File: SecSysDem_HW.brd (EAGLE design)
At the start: 99 x 80 mm, 49 parts, among them IC1 L7805 5V, Q1 2N3904, T1 MOSFET_NCHANNEL_ENHANCEMENT2N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, T2 MOSFET_NCHANNEL_ENHANCEMENT2N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, T3 MOSFET_NCHANNEL_ENHANCEMENT2N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, U1 XPLAINED_MINI_PINOUT, U2 PCF8574_IO_EXPANDER, U4 FT24C512A, U5 MCP4901-E/SN, X1 C-GRID-06-70553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

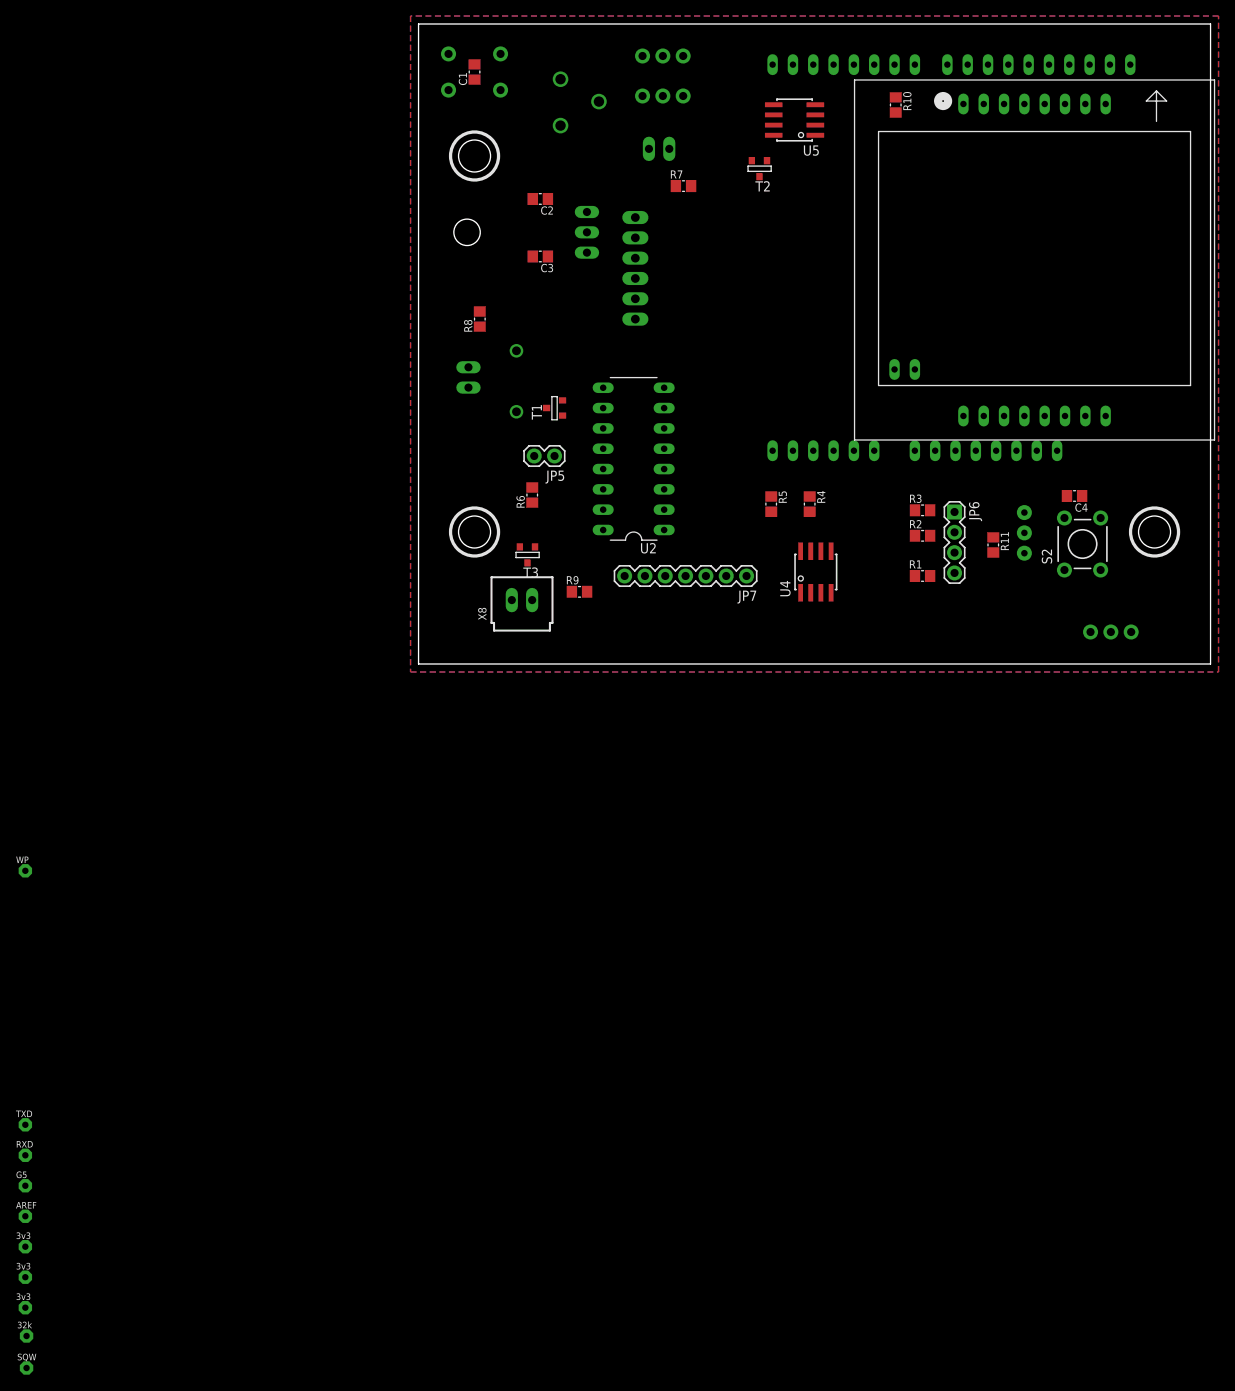
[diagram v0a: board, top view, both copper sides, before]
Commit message: Continued PCB layout. Moved some pin options.
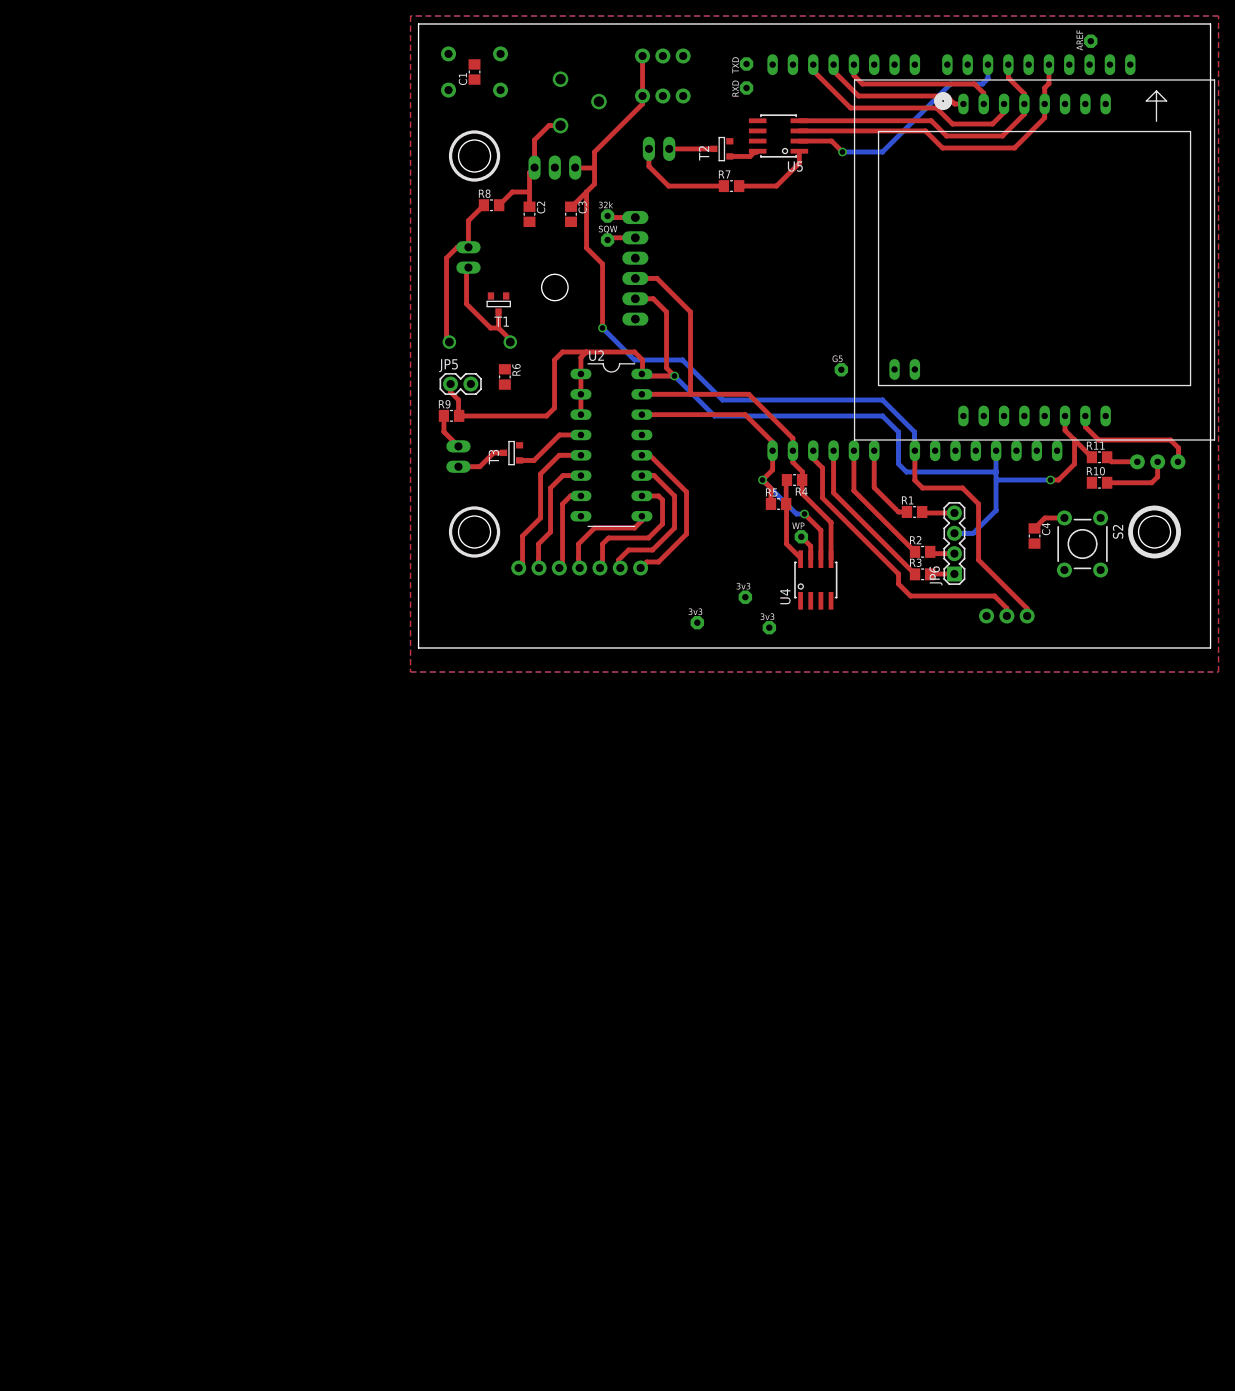
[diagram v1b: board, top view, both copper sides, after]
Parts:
- moved V6 198.3 mm to (84.0, 66.8), turned to 90 degrees
- moved V4 161.0 mm to (41.0, 61.0), turned to 90 degrees
- moved V3 160.3 mm to (41.0, 64.0), turned to 90 degrees
- moved V10 158.6 mm to (23.6, 42.0)
- moved V2 157.7 mm to (23.6, 45.0)
- moved V5 144.2 mm to (52.9, 25.8)
- moved V9 126.0 mm to (43.9, -6.46)
- moved V8 123.8 mm to (40.9, -2.65)
- moved V7 114.6 mm to (34.9, -5.84)
- moved V1 105.6 mm to (47.9, 4.90)
- moved R10 53.7 mm to (85.1, 11.7), turned to 0 degrees
- moved JP7 28.5 mm to (12.5, 1.00), flipped to the bottom
- moved R9 27.2 mm to (4.12, 20.0)
- moved X8 19.6 mm to (4.99, 14.9), flipped to the bottom, turned to 90 degrees
- moved Q1 18.9 mm to (92.4, 14.3), turned to 180 degrees
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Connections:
- net BELL_RINGER: now also U2.4; no longer U1.P$21
- net PUSH_BUTTON: now also U1.P$21; no longer U2.4
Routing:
- net +3V3: track 0.00 -> 168.1 mm, vias 0 -> 2
- net +5V: track 0.00 -> 119.0 mm, vias 0 -> 1
- net I2C_SDA: track 0.00 -> 57.2 mm
- net SPI_SCK: track 0.00 -> 40.0 mm
- net I2C_SCL: track 0.00 -> 40.0 mm, vias 0 -> 2
- net SPI_MOSI: track 0.00 -> 37.1 mm
- net PIR_SENSOR: track 0.00 -> 36.8 mm
- net !DAC_CS: track 0.00 -> 29.7 mm, vias 0 -> 1
- net LCD_DC: track 0.00 -> 29.0 mm
- net KEYPAD_7: track 0.00 -> 20.2 mm
- net N$17: track 0.00 -> 20.0 mm
- net LCD_SS: track 0.00 -> 19.8 mm
- net RGB_BLU: track 0.00 -> 19.7 mm
- net KEYPAD_1: track 0.00 -> 18.9 mm
- net KEYPAD_6: track 0.00 -> 18.9 mm
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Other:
- board size 99 x 80 mm -> 99 x 78 mm

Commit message: Finished PCB layout.
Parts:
- added R12, R13, R14, R15, R16, R17, R18: 10k, Luke:C0805
- moved V7 41.1 mm to (73.8, 7.16)
- moved V9 41.0 mm to (14.8, 22.5)
- moved R10 5.00 mm to (90.1, 11.7)
- moved V8 3.16 mm to (37.9, -1.65)
- moved JP7 2.00 mm to (12.5, -1.00)
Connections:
- net +3V3: now also R12.2, R13.2, R14.2, R15.2, R16.2, R17.2, R18.2
- net KEYPAD_1: now also R12.1
- net KEYPAD_2: now also R13.1
- net KEYPAD_3: now also R14.1
- net KEYPAD_4: now also R15.1
- net KEYPAD_5: now also R16.1
- net KEYPAD_6: now also R17.1
- net KEYPAD_7: now also R18.1
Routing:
- net !RESET_BTN: track 0.00 -> 129.4 mm, vias 0 -> 3
- net DOORLOCK_SOLENOID: track 0.00 -> 90.6 mm, vias 0 -> 1
- net +3V3: track 168.1 -> 254.7 mm, vias 2 -> 5
- net PUSH_BUTTON: track 4.28 -> 82.0 mm
- net LCD_BACKLIGHT: track 0.00 -> 74.5 mm, vias 0 -> 1
- net PHOTORESISTOR: track 0.00 -> 62.3 mm, vias 0 -> 1
- net DOOR_HALL_EFFECT: track 0.00 -> 39.7 mm
- net WINDOW_HALL_EFFECT: track 0.00 -> 37.4 mm
- net I2C_SCL: track 40.0 -> 72.6 mm, vias 2 -> 3
- net N$14: track 0.00 -> 7.67 mm
- net +5V: track 119.0 -> 126.3 mm
- net N$15: track 0.00 -> 6.69 mm
- net N$7: track 8.51 -> 3.51 mm
- net KEYPAD_5: track 17.5 -> 22.1 mm
- net KEYPAD_4: track 12.7 -> 17.3 mm
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
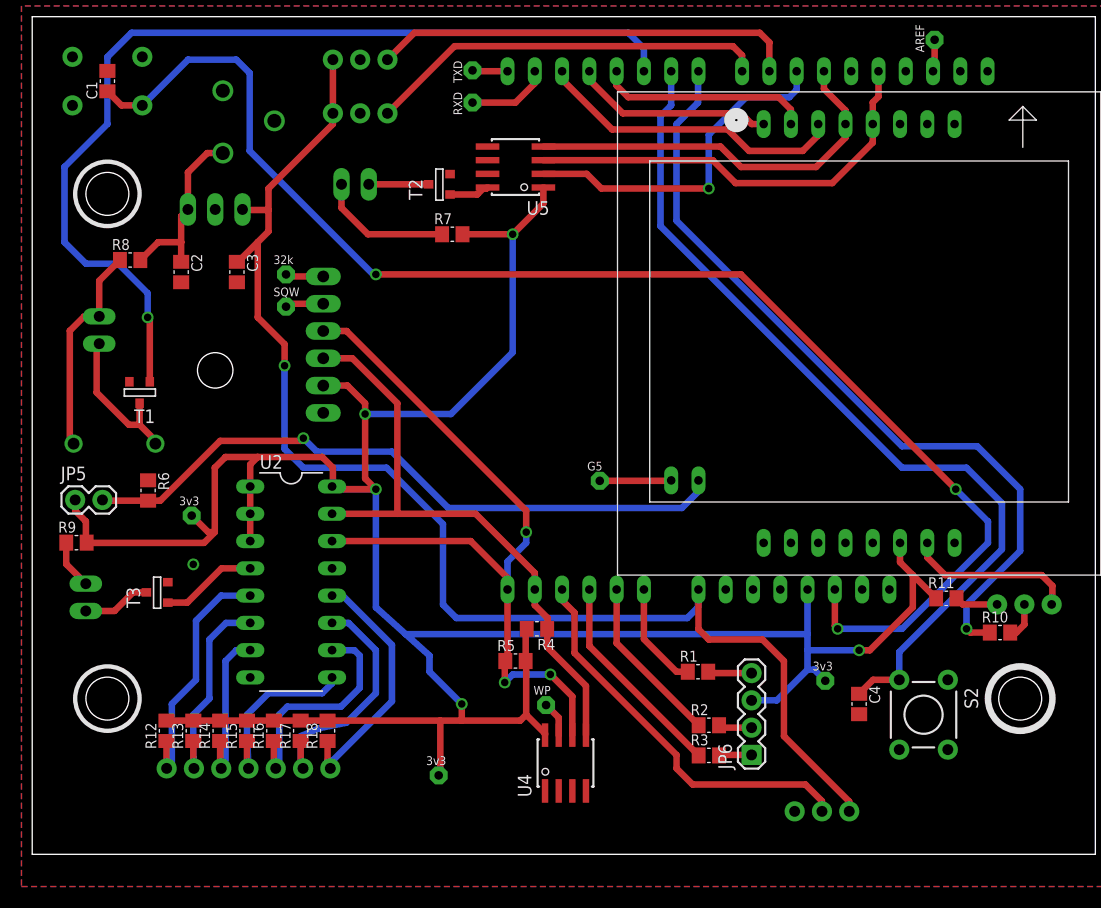
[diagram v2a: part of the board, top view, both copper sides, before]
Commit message: Refinished board layout with silkscreen.
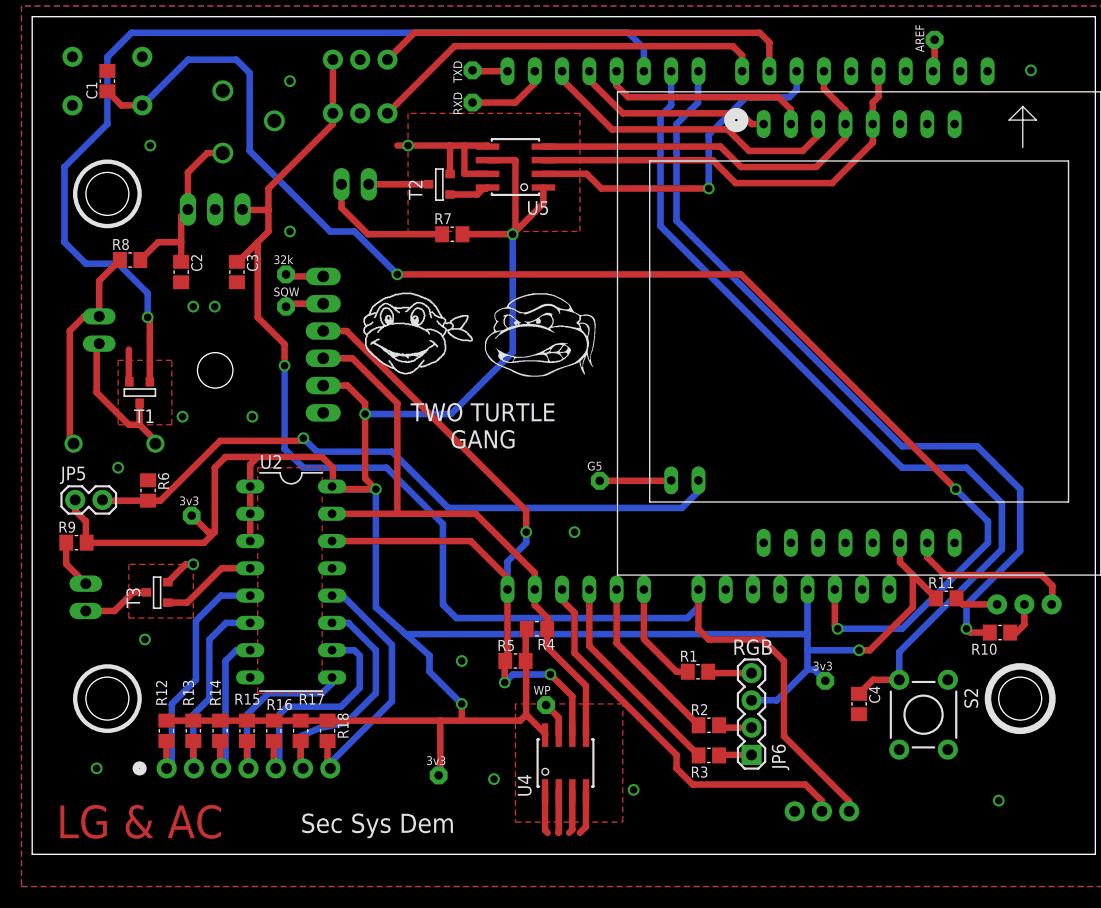
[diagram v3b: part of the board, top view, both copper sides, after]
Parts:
- added U$1: (no value), Luke:NINJA_TURTLE1
- added U$4: (no value), Luke:NINJA_TURTLE2
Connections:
- net +3V3: now also U5.6
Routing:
- net GND: track 0.00 -> 38.1 mm, vias 1 -> 18
- net +3V3: track 254.7 -> 264.5 mm
- added copper zone on layer 1, net N$21
- added copper zone on layer 1, net N$23
- added copper zone on layer 1, net N$24
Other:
- board text added: "+5V"
- board text added: "- +"
- board text added: "5V"
- board text added: "BELL"
- board text added: "GND"
- board text added: "H.DOOR"
- board text added: "H.WIND"
- board text added: "KEYPAD"
- board text added: "LG & AC"
- board text added: "LOCK"
- board text added: "OUT"
- board text added: "PHOTORES"
- board text added: "PIR"
- board text added: "PIR SENS"
- board text added: "RESET"
- board text added: "RGB"
- board text added: "SPEAKER"
- board text added: "Sec Sys Dem"
- board text added: "TWO TURTLE GANG"

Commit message: Change bell to +5v
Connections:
- net +3V3: no longer R9.2
- net +5V: now also R9.2
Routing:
- net +5V: track 126.3 -> 151.4 mm, vias 1 -> 2
- net +3V3: track 264.5 -> 258.1 mm
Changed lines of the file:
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@@
 <wire x1="33" y1="27" x2="25.25" y2="27" width="0.6096" layer="16"/>
 <wire x1="25.25" y1="27" x2="23.5" y2="28.75" width="0.6096" layer="16"/>
-<wire x1="23.5" y1="28.75" x2="23.5" y2="36.5" width="0.6096" layer="16"/>
+<wire x1="23.5" y1="28.75" x2="23.5" y2="29" width="0.6096" layer="16"/>
 <via x="23.5" y="36.5" extent="1-16" drill="0.7"/>
+<wire x1="23.5" y1="29" x2="23.5" y2="36.5" width="0.6096" layer="16"/>
 <wire x1="23.5" y1="36.5" x2="23.5" y2="38.5" width="0.6096" layer="1"/>
 <wire x1="23.5" y1="38.5" x2="21" y2="41" width="0.6096" layer="1"/>
@@
 <wire x1="39.5" y1="13" x2="38.25" y2="14.25" width="0.6096" layer="16"/>
 <wire x1="38.25" y1="14.25" x2="38.25" y2="21.75" width="0.6096" layer="16"/>
+<contactref element="R9" pad="2"/>
+<wire x1="5.07" y1="20.02" x2="5.09" y2="20" width="0.6096" layer="1"/>
+<wire x1="5.09" y1="20" x2="12" y2="20" width="0.6096" layer="1"/>
+<via x="12" y="20" extent="1-16" drill="0.7"/>
+<wire x1="12" y1="20" x2="12" y2="25" width="0.6096" layer="16"/>
+<wire x1="12" y1="25" x2="16" y2="29" width="0.6096" layer="16"/>
+<wire x1="16" y1="29" x2="23.5" y2="29" width="0.6096" layer="16"/>
 </signal>
 <signal name="+3V3">
@@
 <contactref element="V8" pad="P$1"/>
 <contactref element="V9" pad="P$1"/>
-<contactref element="R9" pad="2"/>
 <contactref element="R7" pad="2"/>
 <contactref element="R11" pad="1"/>
@@
 <wire x1="82.005" y1="17.005" x2="80.81" y2="18.2" width="0.6096" layer="1"/>
 <wire x1="80.81" y1="18.2" x2="80.81" y2="20" width="0.6096" layer="1"/>
-<wire x1="5.07" y1="20.02" x2="5" y2="20.09" width="0.6096" layer="1"/>
-<wire x1="5" y1="20.09" x2="5" y2="22" width="0.6096" layer="1"/>
-<wire x1="5" y1="22" x2="4" y2="23" width="0.6096" layer="1"/>
 <wire x1="4" y1="23" x2="4" y2="24" width="0.6096" layer="1"/>
 <wire x1="20.3" y1="20.17" x2="20.3" y2="22.71" width="0.6096" layer="1"/>
@@
 <wire x1="21" y1="28" x2="20.3" y2="27.3" width="0.6096" layer="1"/>
 <wire x1="20.3" y1="27.3" x2="20.3" y2="25.25" width="0.6096" layer="1"/>
-<wire x1="5.07" y1="20.02" x2="5.09" y2="20" width="0.6096" layer="1"/>
-<wire x1="5.09" y1="20" x2="16" y2="20" width="0.6096" layer="1"/>
-<wire x1="16" y1="20" x2="17" y2="21" width="0.6096" layer="1"/>
-<wire x1="17" y1="21" x2="17" y2="27" width="0.6096" layer="1"/>
-<wire x1="17" y1="27" x2="18" y2="28" width="0.6096" layer="1"/>
 <wire x1="18" y1="28" x2="21" y2="28" width="0.6096" layer="1"/>
 <wire x1="66.985" y1="5.335" x2="69.335" y2="5.335" width="0.6096" layer="16"/>
@@
 <wire x1="73.85" y1="7.16" x2="72.81" y2="8.2" width="0.6096" layer="16"/>
 <wire x1="72.81" y1="8.2" x2="72.2" y2="8.2" width="0.6096" layer="16"/>
-<wire x1="14.85" y1="22.54" x2="16.39" y2="21" width="0.6096" layer="1"/>
-<wire x1="16.39" y1="21" x2="17" y2="21" width="0.6096" layer="1"/>
 <contactref element="U5" pad="6"/>
 <wire x1="42.4" y1="55.635" x2="45" y2="55.635" width="0.6096" layer="1"/>
@@
 <wire x1="45" y1="49" x2="44.74" y2="49" width="0.6096" layer="1"/>
 <wire x1="44.74" y1="49" x2="44.74" y2="48.74" width="0.6096" layer="1"/>
+<wire x1="4" y1="23" x2="5" y2="22" width="0.6096" layer="1"/>
+<wire x1="5" y1="22" x2="13" y2="22" width="0.6096" layer="1"/>
+<wire x1="13" y1="22" x2="14" y2="22" width="0.6096" layer="1"/>
+<wire x1="14" y1="22" x2="14.54" y2="22.54" width="0.6096" layer="1"/>
+<wire x1="14.54" y1="22.54" x2="14.85" y2="22.54" width="0.6096" layer="1"/>
+<wire x1="18" y1="28" x2="13" y2="23" width="0.6096" layer="1"/>
+<wire x1="13" y1="23" x2="13" y2="22" width="0.6096" layer="1"/>
 </signal>
 <signal name="PHOTORESISTOR">
